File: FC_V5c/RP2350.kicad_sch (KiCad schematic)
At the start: 27 parts, among them U11 W25Q128JVS, U18 RP2350_60QFN, Y1 ABM8-272-T3

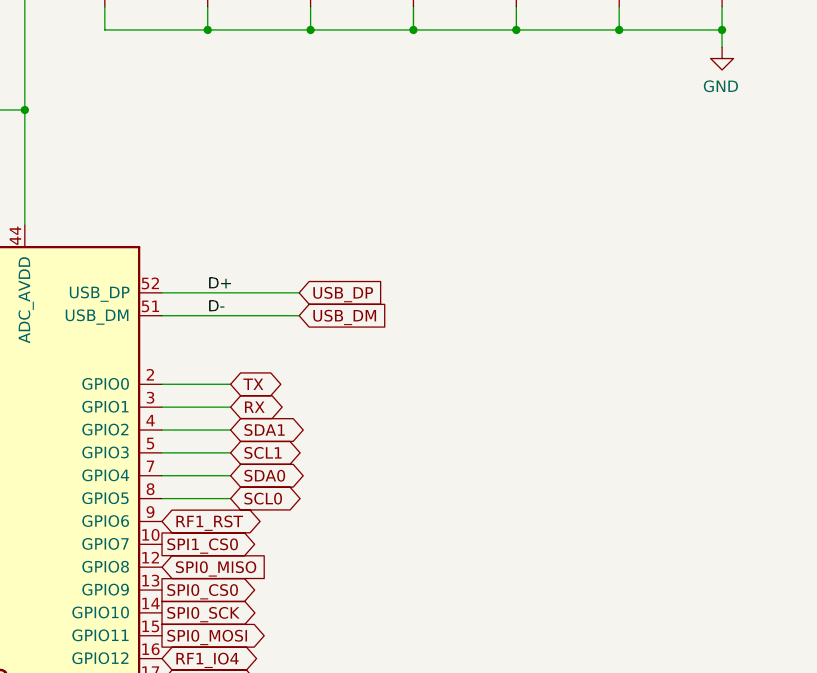
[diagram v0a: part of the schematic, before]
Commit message: Updated I2C Pullups to 4.7k
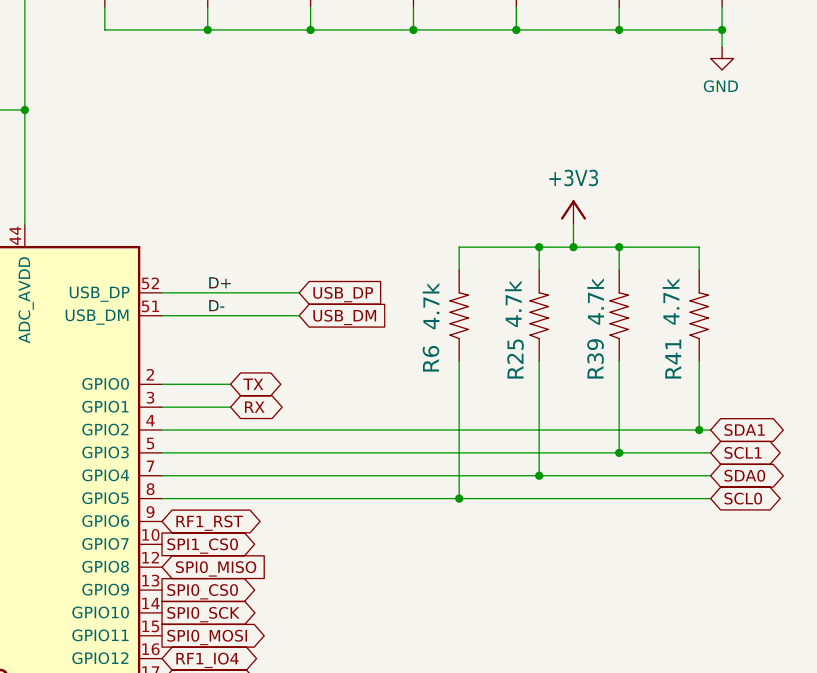
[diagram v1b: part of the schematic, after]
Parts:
- added R25, R39, R41, R6: 4.7k, Resistor_SMD:R_0603_1608Metric, symbol mainboard:RESISTOR0603
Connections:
- net +3V3: now also R25.2, R39.2, R41.2, R6.2
- net SCL0: now also R6.1
- net SCL1: now also R39.1
- net SDA0: now also R25.1
- net SDA1: now also R41.1

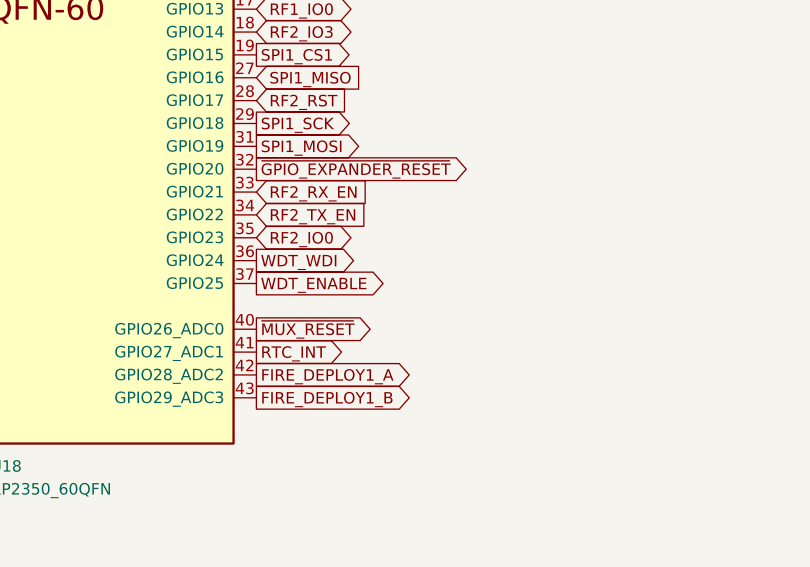
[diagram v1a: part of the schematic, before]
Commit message: Removed WDT Loadswitch
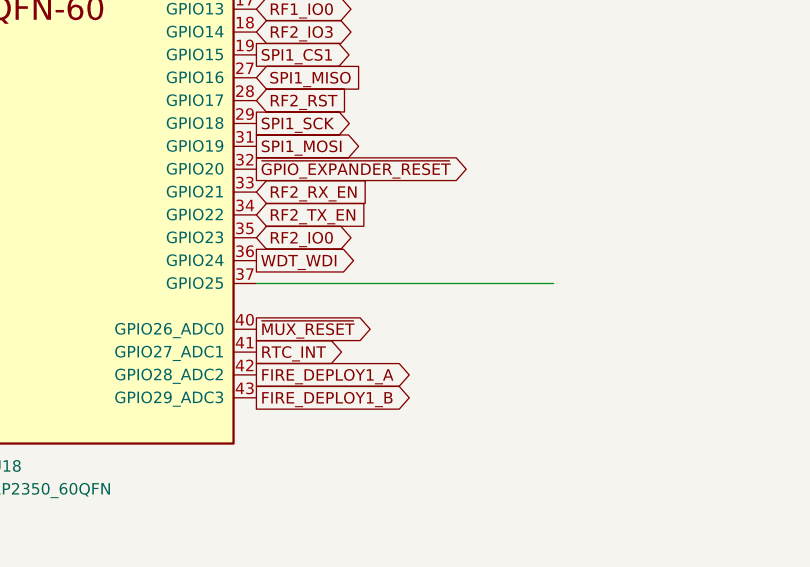
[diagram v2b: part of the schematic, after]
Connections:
- net WDT_ENABLE: no longer names the net of U18.37 (GPIO25)
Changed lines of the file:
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@@
+	(wire
+		(pts
+			(xy 242.57 135.89) (xy 209.55 135.89)
+		)
+		(stroke
+			(width 0)
+			(type default)
+		)
+	)
 	(wire
 		(pts
@@
 			(effects
 				(font
-					(size 1.27 1.27)
-				)
-				(justify left)
-				(hide yes)
-			)
-		)
-	)
-	(global_label "WDT_ENABLE"
-		(shape output)
-		(at 209.55 135.89 0)
-		(fields_autoplaced yes)
-		(effects
-			(font
-				(size 1.27 1.27)
-			)
-			(justify left)
-		)
-		(property "Intersheetrefs" "${INTERSHEET_REFS}"
-			(at 224.207 135.89 0)
-			(effects
-				(font

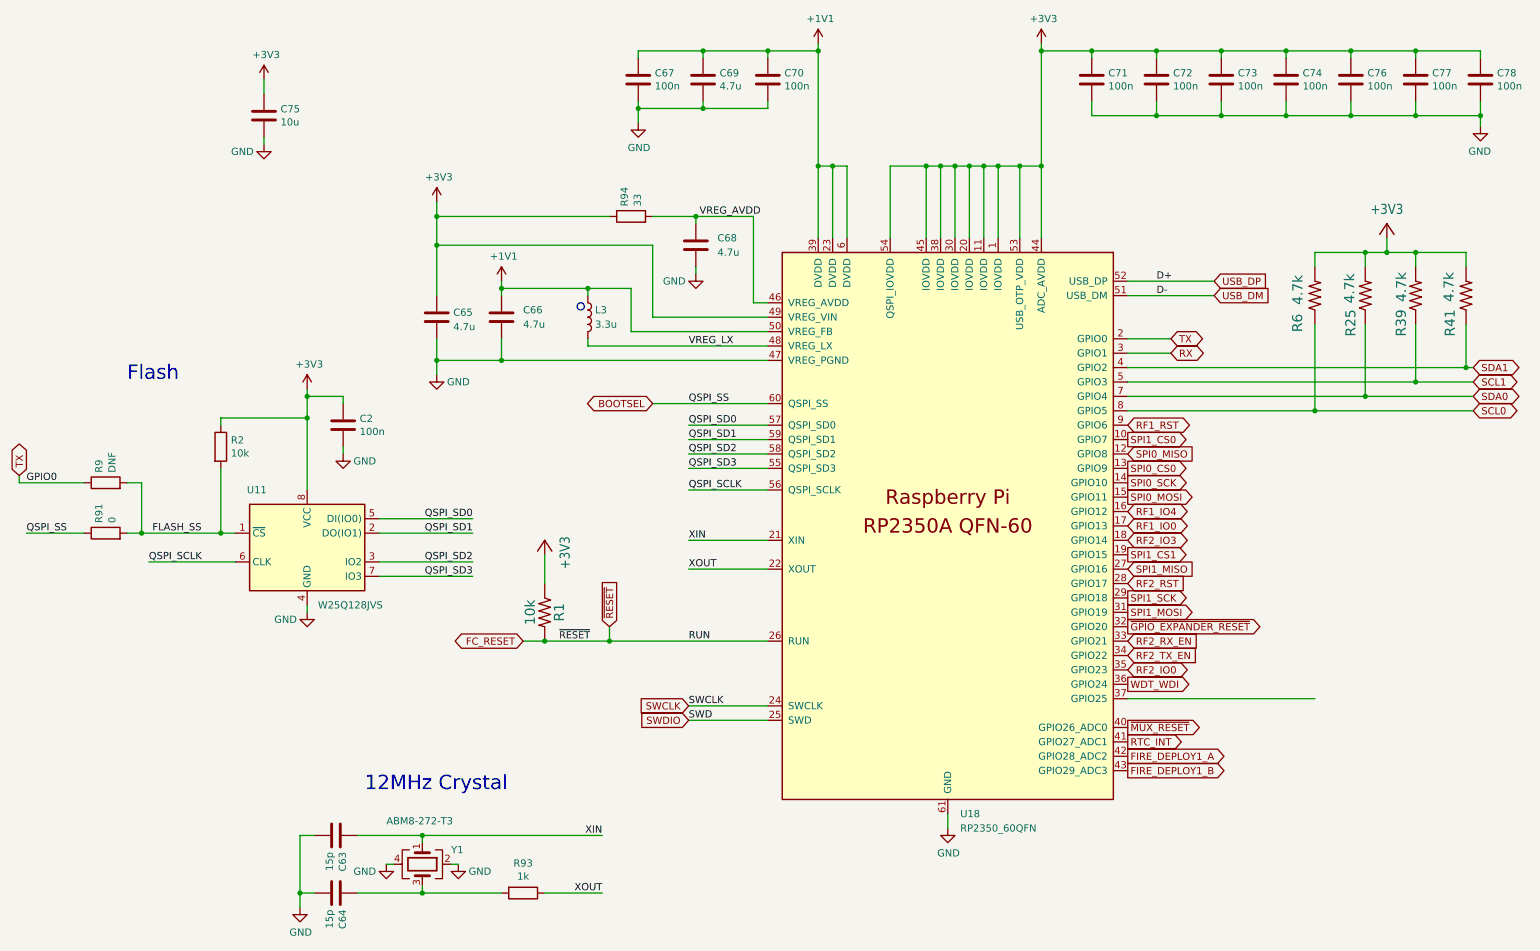
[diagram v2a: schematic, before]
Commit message: Finished Wiring PSRAM Memory
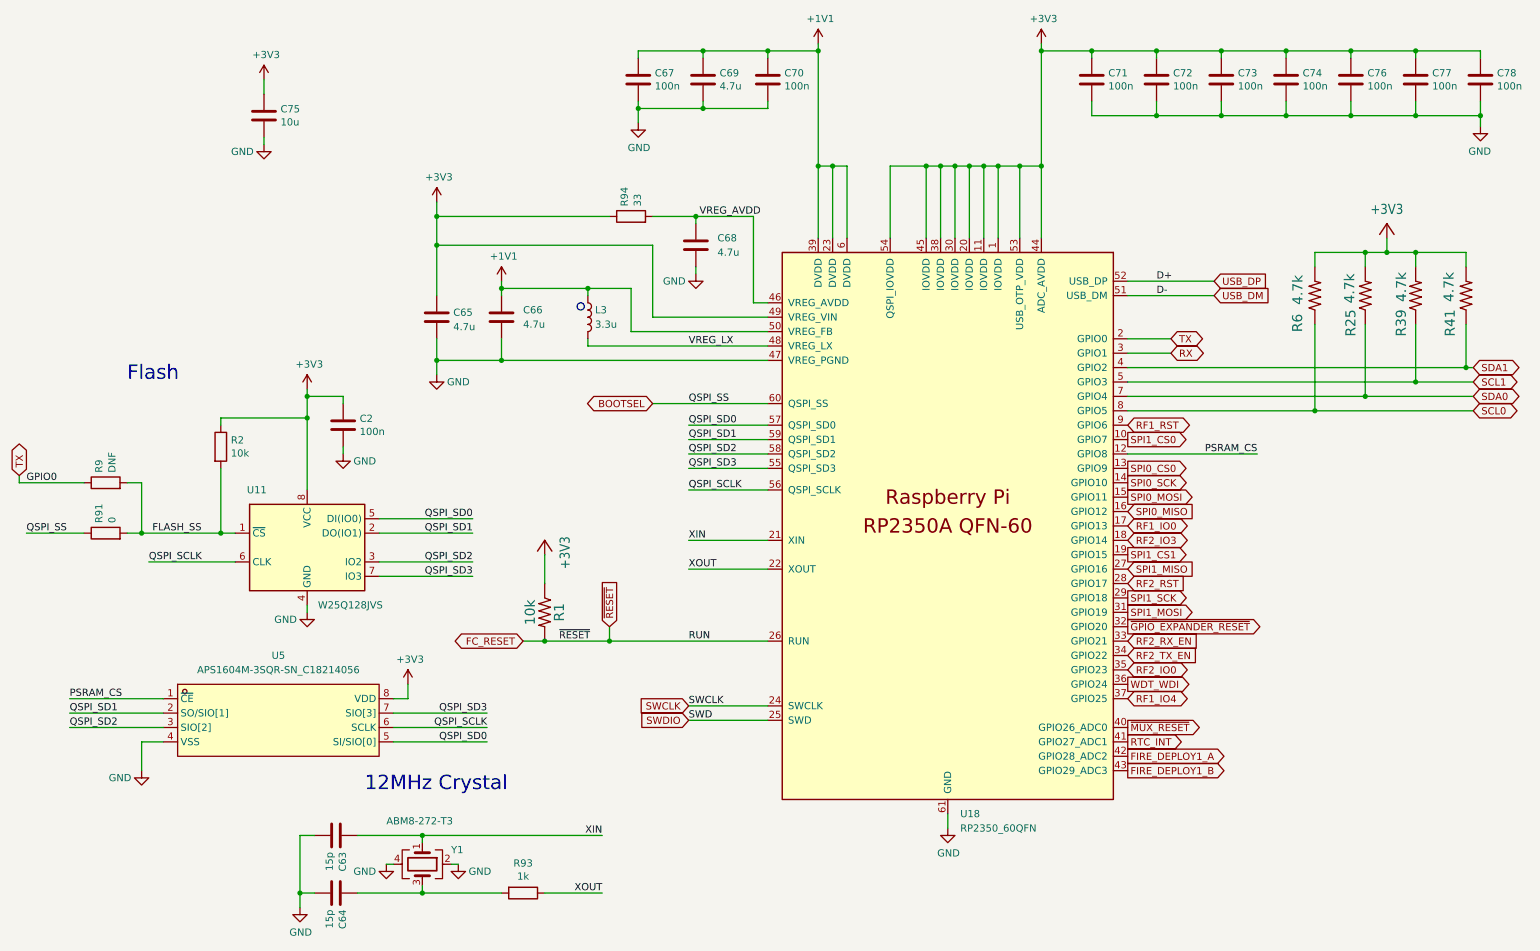
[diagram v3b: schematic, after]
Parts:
- added U5: APS1604M-3SQR-SN_C18214056, easyeda2kicad:SOIC-8_L4.9-W3.9-P1.27-LS6.0-BL, symbol easyeda2kicad:APS1604M-3SQR-SN_C18214056
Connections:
- net +3V3: now also U5.8 (VDD)
- net GND: now also U5.4 (VSS)
- net QSPI_SCLK: now also U5.6 (SCLK)
- net QSPI_SD0: now also U5.5 (SI/SIO[0])
- net QSPI_SD1: now also U5.2 (SO/SIO[1])
- net QSPI_SD2: now also U5.3 (SIO[2])
- net QSPI_SD3: now also U5.7 (SIO[3])
- net RF1_IO4: now also U18.37 (GPIO25); no longer U18.16 (GPIO12)
- net SPI0_MISO: now also U18.16 (GPIO12); no longer U18.12 (GPIO8)
- new net PSRAM_CS: U18.12 (GPIO8), U5.1 (~{CE})
